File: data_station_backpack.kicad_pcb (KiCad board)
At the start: 2 copper layers, 68.6 x 53.3 mm, 37 parts, among them J1 Conn_01x02_Male, J10 Conn_01x02_Male, J11 Conn_01x03_Male, J12 Conn_01x06_Male, J13 Conn_01x06_Male, J14 Conn_01x08_Male, J16 Conn_01x08_Male, J17 Conn_01x10_Male, J2 Conn_01x02_Male, J3 Conn_01x06_Male, J4 Conn_01x02_Male, J5 Conn_01x02_Male, J6 Conn_01x02_Male, J7 Conn_01x02_Male, J8 Conn_01x06_Male, J9 Conn_01x02_Male, Q1 2N2222, Q2 2N2222, U1 LM7805_TO220

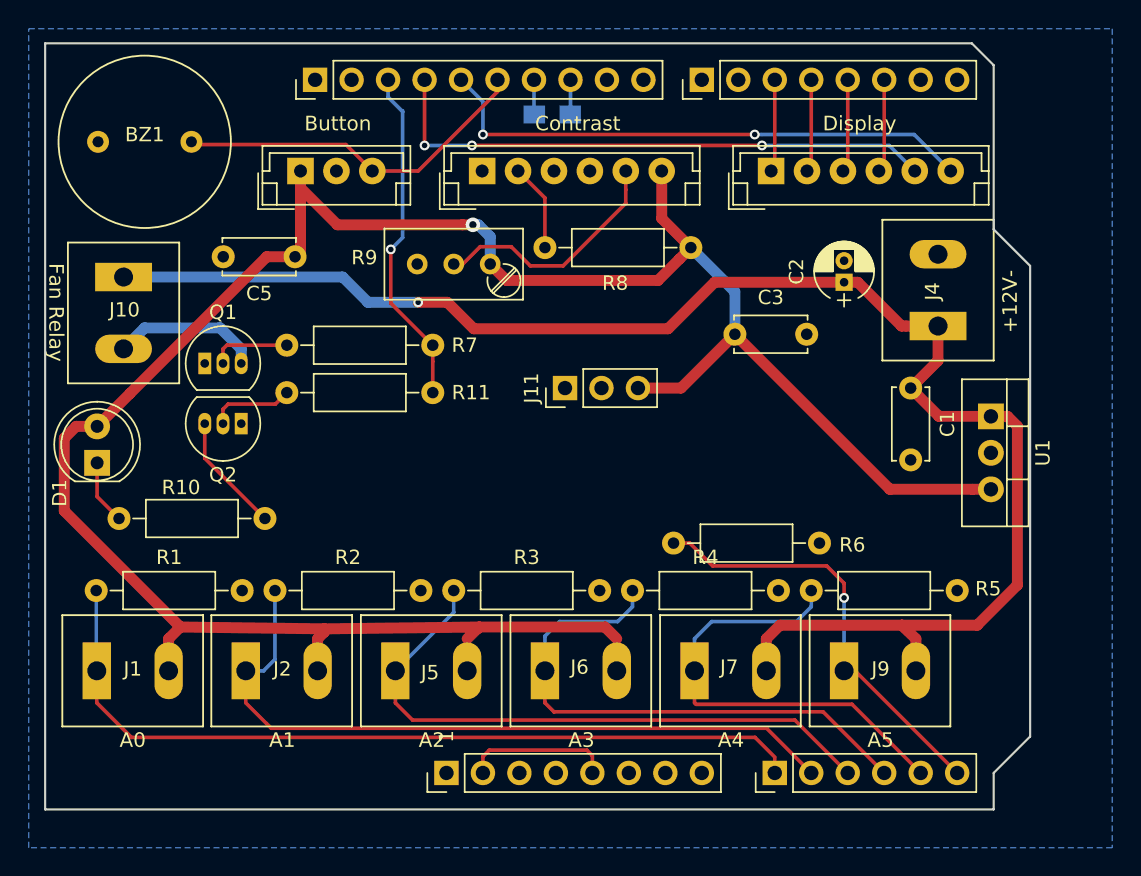
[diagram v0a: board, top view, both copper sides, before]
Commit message: Updated to reflect actual order
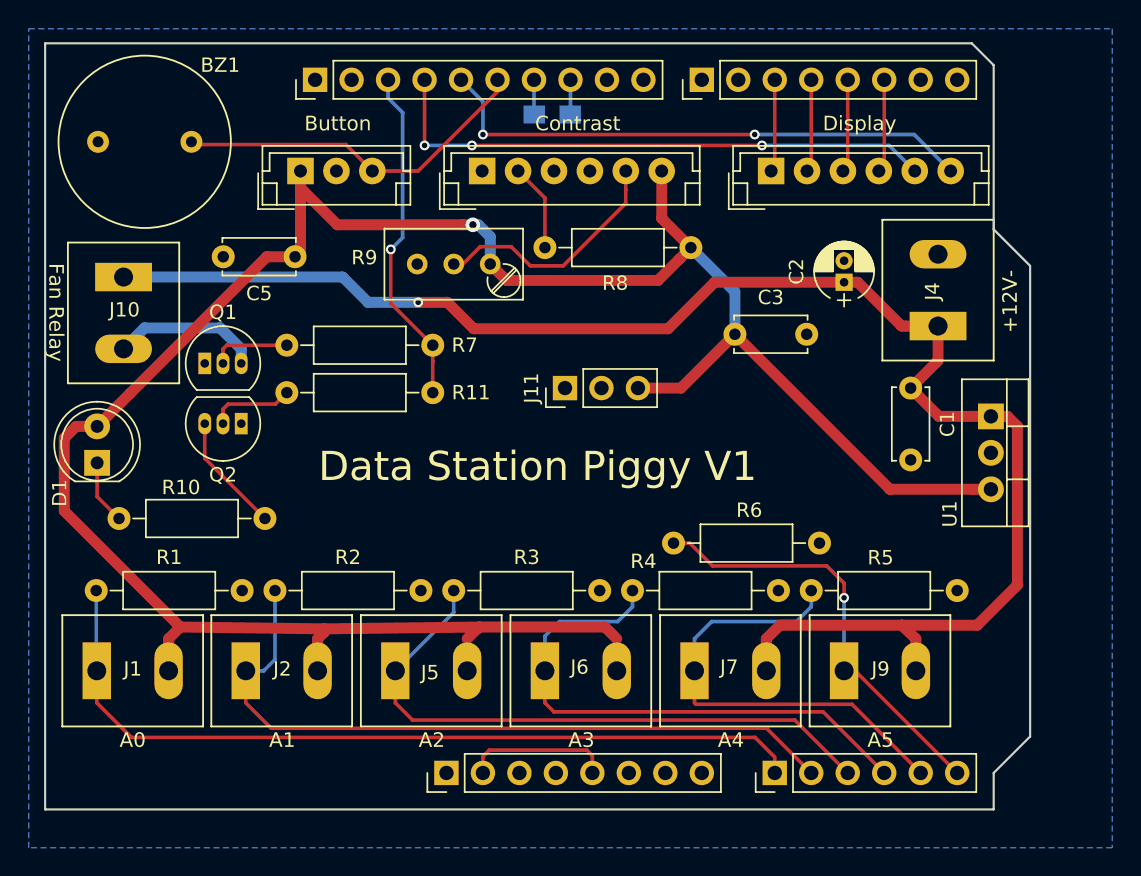
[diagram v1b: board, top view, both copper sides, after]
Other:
- board text added: "Data Station Piggy V1"
- board text removed: "1"
